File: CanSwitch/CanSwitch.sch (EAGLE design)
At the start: 17 parts

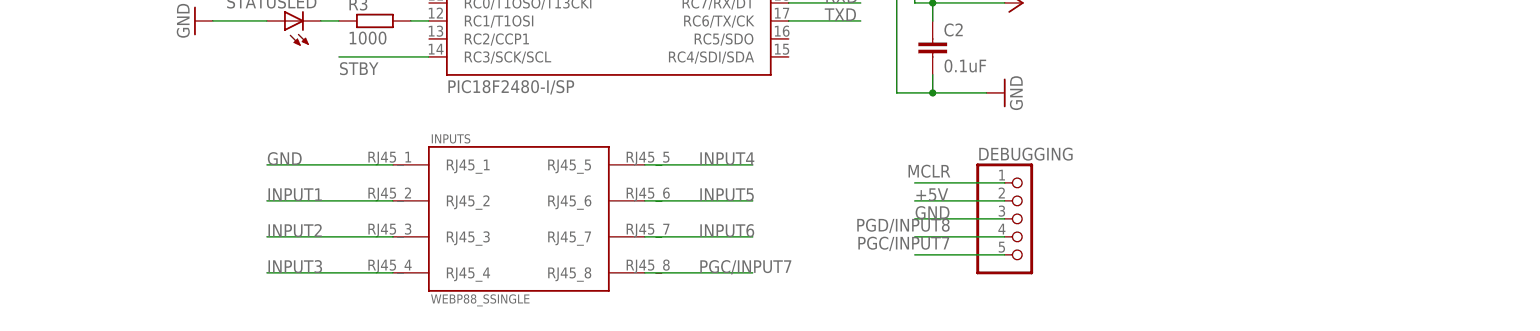
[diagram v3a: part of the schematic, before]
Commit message: #17 replaced RJ45 for inputs with 5 PTR 2pins   - RJ45 dropped and up to 5 individual PTR inputs I already bought   added to the board so that they can be connected if needed   - has the advantage of simple board for just 1 switch - the same as   before, but I can really wire up all 8 inputs of a can switch now if   needed   - also better work with cables using this big inputs switch   - moved things around on the board, did not change dimension of the   board in the end   - moved double RJ45 a bit to the left   - rewired CAN lines, used thick line as well this time   - updated isolation for GND copper boards   - all wired up, perhaps just fine tune labels next time
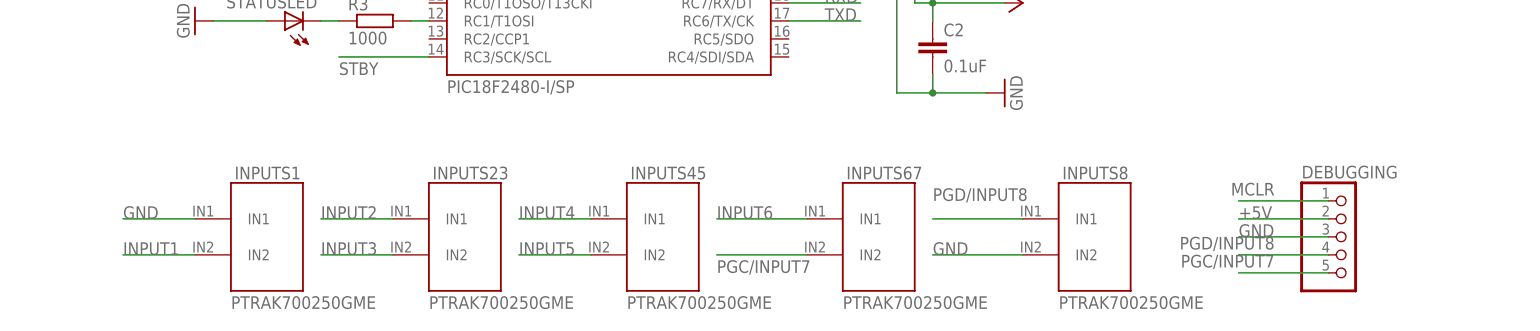
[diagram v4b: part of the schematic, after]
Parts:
- removed INPUTS: WEBP88_SSINGLE, PoJD:WEBP88_SSINGLE
- added INPUTS1, INPUTS23, INPUTS45, INPUTS67, INPUTS8: PTRAK700250GME, PoJD:PTRAK700250GME
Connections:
- net GND: now also INPUTS1.IN1, INPUTS8.IN2; no longer INPUTS.RJ45_1
- net INPUT1: now also INPUTS1.IN2; no longer INPUTS.RJ45_2
- net INPUT2: now also INPUTS23.IN1; no longer INPUTS.RJ45_3
- net INPUT3: now also INPUTS23.IN2; no longer INPUTS.RJ45_4
- net INPUT4: now also INPUTS45.IN1; no longer INPUTS.RJ45_5
- net INPUT5: now also INPUTS45.IN2; no longer INPUTS.RJ45_6
- net INPUT6: now also INPUTS67.IN1; no longer INPUTS.RJ45_7
- net PGC/INPUT7: now also INPUTS67.IN2; no longer INPUTS.RJ45_8
- net PGD/INPUT8: now also INPUTS8.IN1
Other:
- moved on the sheet: DEBUGGING
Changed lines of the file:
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@@
 <part name="C3" library="rcl" deviceset="C-EU" device="050-025X075" value="0.1uF"/>
 <part name="XTAL" library="special" deviceset="XTAL/S" device="" value="16MHz"/>
-<part name="INPUTS" library="PoJD" deviceset="WEBP88_S" device="SINGLE"/>
+<part name="INPUTS23" library="PoJD" deviceset="PTRAK700250" device="GME"/>
+<part name="INPUTS45" library="PoJD" deviceset="PTRAK700250" device="GME"/>
+<part name="INPUTS67" library="PoJD" deviceset="PTRAK700250" device="GME"/>
+<part name="INPUTS8" library="PoJD" deviceset="PTRAK700250" device="GME"/>
+<part name="INPUTS1" library="PoJD" deviceset="PTRAK700250" device="GME"/>
 </parts>
 <sheets>
@@
 <instances>
 <instance part="CHIP" gate="G$1" x="-76.2" y="86.36"/>
-<instance part="DEBUGGING" gate="A" x="-17.78" y="48.26"/>
+<instance part="DEBUGGING" gate="A" x="27.94" y="45.72"/>
 <instance part="RJ45CONNECTOR" gate="G$1" x="-55.88" y="124.46"/>
 <instance part="MCP2561" gate="G$1" x="20.32" y="96.52"/>
@@
 <instance part="C3" gate="G$1" x="-20.32" y="99.06"/>
 <instance part="XTAL" gate="G$1" x="-119.38" y="93.98" rot="R90"/>
-<instance part="INPUTS" gate="G$1" x="-88.9" y="48.26"/>
+<instance part="INPUTS23" gate="G$1" x="-96.52" y="45.72"/>
+<instance part="INPUTS45" gate="G$1" x="-68.58" y="45.72"/>
+<instance part="INPUTS67" gate="G$1" x="-38.1" y="45.72"/>
+<instance part="INPUTS8" gate="G$1" x="-7.62" y="45.72"/>
+<instance part="INPUTS1" gate="G$1" x="-124.46" y="45.72"/>
 </instances>
 <busses>
@@
 <segment>
 <pinref part="DEBUGGING" gate="A" pin="2"/>
-<wire x1="-20.32" y1="50.8" x2="-33.02" y2="50.8" width="0.1524" layer="91"/>
-<label x="-33.02" y="50.8" size="1.778" layer="95"/>
+<wire x1="25.4" y1="48.26" x2="12.7" y2="48.26" width="0.1524" layer="91"/>
+<label x="12.7" y="48.26" size="1.778" layer="95"/>
 </segment>
 <segment>
@@
 <segment>
 <pinref part="DEBUGGING" gate="A" pin="3"/>
-<wire x1="-20.32" y1="48.26" x2="-33.02" y2="48.26" width="0.1524" layer="91"/>
-<label x="-33.02" y="48.26" size="1.778" layer="95"/>
+<wire x1="25.4" y1="45.72" x2="12.7" y2="45.72" width="0.1524" layer="91"/>
+<label x="12.7" y="45.72" size="1.778" layer="95"/>
 </segment>
 <segment>
@@
 </segment>
 <segment>
-<pinref part="INPUTS" gate="G$1" pin="RJ45_1"/>
-<wire x1="-106.68" y1="55.88" x2="-124.46" y2="55.88" width="0.1524" layer="91"/>
-<label x="-124.46" y="55.88" size="1.778" layer="95"/>
+<pinref part="INPUTS8" gate="G$1" pin="IN2"/>
+<wire x1="-17.78" y1="43.18" x2="-30.48" y2="43.18" width="0.1524" layer="91"/>
+<label x="-30.48" y="43.18" size="1.778" layer="95"/>
+</segment>
+<segment>
+<pinref part="INPUTS1" gate="G$1" pin="IN1"/>
+<wire x1="-134.62" y1="48.26" x2="-144.78" y2="48.26" width="0.1524" layer="91"/>
+<label x="-144.78" y="48.26" size="1.778" layer="95"/>
 </segment>
 </net>
@@
 <segment>
 <pinref part="DEBUGGING" gate="A" pin="1"/>
-<wire x1="-33.02" y1="53.34" x2="-20.32" y2="53.34" width="0.1524" layer="91"/>
-<label x="-27.94" y="55.88" size="1.778" layer="95" rot="R180"/>
+<wire x1="12.7" y1="50.8" x2="25.4" y2="50.8" width="0.1524" layer="91"/>
+<label x="17.78" y="53.34" size="1.778" layer="95" rot="R180"/>
 </segment>
 <segment>
@@
 </segment>
 <segment>
-<pinref part="INPUTS" gate="G$1" pin="RJ45_5"/>
-<wire x1="-71.12" y1="55.88" x2="-55.88" y2="55.88" width="0.1524" layer="91"/>
-<label x="-63.5" y="55.88" size="1.778" layer="95"/>
+<pinref part="INPUTS45" gate="G$1" pin="IN1"/>
+<wire x1="-78.74" y1="48.26" x2="-88.9" y2="48.26" width="0.1524" layer="91"/>
+<label x="-88.9" y="48.26" size="1.778" layer="95"/>
 </segment>
 </net>
@@
 </segment>
 <segment>
-<pinref part="INPUTS" gate="G$1" pin="RJ45_4"/>
-<wire x1="-106.68" y1="40.64" x2="-124.46" y2="40.64" width="0.1524" layer="91"/>
-<label x="-124.46" y="40.64" size="1.778" layer="95"/>
+<pinref part="INPUTS23" gate="G$1" pin="IN2"/>
+<wire x1="-106.68" y1="43.18" x2="-116.84" y2="43.18" width="0.1524" layer="91"/>
+<label x="-116.84" y="43.18" size="1.778" layer="95"/>
 </segment>
 </net>
@@
 </segment>
 <segment>
-<pinref part="INPUTS" gate="G$1" pin="RJ45_3"/>
-<wire x1="-106.68" y1="45.72" x2="-124.46" y2="45.72" width="0.1524" layer="91"/>
-<label x="-124.46" y="45.72" size="1.778" layer="95"/>
+<pinref part="INPUTS23" gate="G$1" pin="IN1"/>
+<wire x1="-106.68" y1="48.26" x2="-116.84" y2="48.26" width="0.1524" layer="91"/>
+<label x="-116.84" y="48.26" size="1.778" layer="95"/>
 </segment>
 </net>
@@
 </segment>
 <segment>
-<pinref part="INPUTS" gate="G$1" pin="RJ45_2"/>
-<wire x1="-106.68" y1="50.8" x2="-124.46" y2="50.8" width="0.1524" layer="91"/>
-<label x="-124.46" y="50.8" size="1.778" layer="95"/>
+<pinref part="INPUTS1" gate="G$1" pin="IN2"/>
+<wire x1="-134.62" y1="43.18" x2="-144.78" y2="43.18" width="0.1524" layer="91"/>
+<label x="-144.78" y="43.18" size="1.778" layer="95"/>
 </segment>
 </net>
@@
 </segment>
 <segment>
-<pinref part="INPUTS" gate="G$1" pin="RJ45_6"/>
-<wire x1="-71.12" y1="50.8" x2="-55.88" y2="50.8" width="0.1524" layer="91"/>
-<label x="-63.5" y="50.8" size="1.778" layer="95"/>
+<pinref part="INPUTS45" gate="G$1" pin="IN2"/>
+<wire x1="-78.74" y1="43.18" x2="-88.9" y2="43.18" width="0.1524" layer="91"/>
+<label x="-88.9" y="43.18" size="1.778" layer="95"/>
 </segment>
 </net>
@@
 </segment>
 <segment>
-<pinref part="INPUTS" gate="G$1" pin="RJ45_7"/>
-<wire x1="-71.12" y1="45.72" x2="-55.88" y2="45.72" width="0.1524" layer="91"/>
-<label x="-63.5" y="45.72" size="1.778" layer="95"/>
+<pinref part="INPUTS67" gate="G$1" pin="IN1"/>
+<wire x1="-48.26" y1="48.26" x2="-60.96" y2="48.26" width="0.1524" layer="91"/>
+<label x="-60.96" y="48.26" size="1.778" layer="95"/>
 </segment>
 </net>
@@
 </segment>
 <segment>
-<pinref part="INPUTS" gate="G$1" pin="RJ45_8"/>
-<wire x1="-71.12" y1="40.64" x2="-55.88" y2="40.64" width="0.1524" layer="91"/>
-<label x="-63.5" y="40.64" size="1.778" layer="95"/>
-</segment>
-<segment>
 <pinref part="DEBUGGING" gate="A" pin="5"/>
-<wire x1="-20.32" y1="43.18" x2="-33.02" y2="43.18" width="0.1524" layer="91"/>
-<label x="-27.94" y="45.72" size="1.778" layer="95" rot="R180"/>
+<wire x1="25.4" y1="40.64" x2="12.7" y2="40.64" width="0.1524" layer="91"/>
+<label x="17.78" y="43.18" size="1.778" layer="95" rot="R180"/>
+</segment>
+<segment>
+<pinref part="INPUTS67" gate="G$1" pin="IN2"/>
+<wire x1="-48.26" y1="43.18" x2="-60.96" y2="43.18" width="0.1524" layer="91"/>
+<label x="-60.96" y="40.64" size="1.778" layer="95"/>
 </segment>
 </net>
@@
 <segment>
 <pinref part="DEBUGGING" gate="A" pin="4"/>
-<wire x1="-20.32" y1="45.72" x2="-33.02" y2="45.72" width="0.1524" layer="91"/>
-<label x="-27.94" y="48.26" size="1.778" layer="95" rot="R180"/>
-</segment>
-</net>
+<wire x1="25.4" y1="43.18" x2="12.7" y2="43.18" width="0.1524" layer="91"/>
+<label x="17.78" y="45.72" size="1.778" layer="95" rot="R180"/>
+</segment>
+<segment>
+<pinref part="INPUTS8" gate="G$1" pin="IN1"/>
+<wire x1="-17.78" y1="48.26" x2="-30.48" y2="48.26" width="0.1524" layer="91"/>
+<label x="-30.48" y="50.8" size="1.778" layer="95"/>
+</segment>
+</net>
